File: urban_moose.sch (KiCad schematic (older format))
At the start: 52 parts, among them P1 SWD, P2 EXT, P3 ANT, Q1 MOSFET_N, Q2 MOSFET_N, SW1 SW_PUSH, U1 nRF51822-QFAA, U2 DS18B20, U3 BMP180, U4 Si1145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

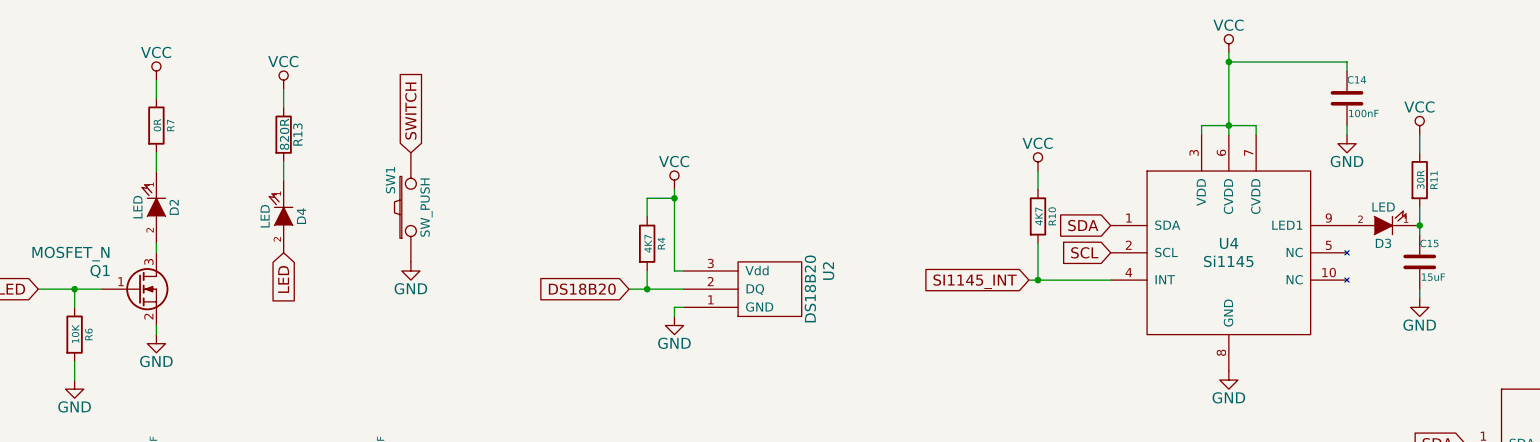
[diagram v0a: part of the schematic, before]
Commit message: Fixes to match library changes
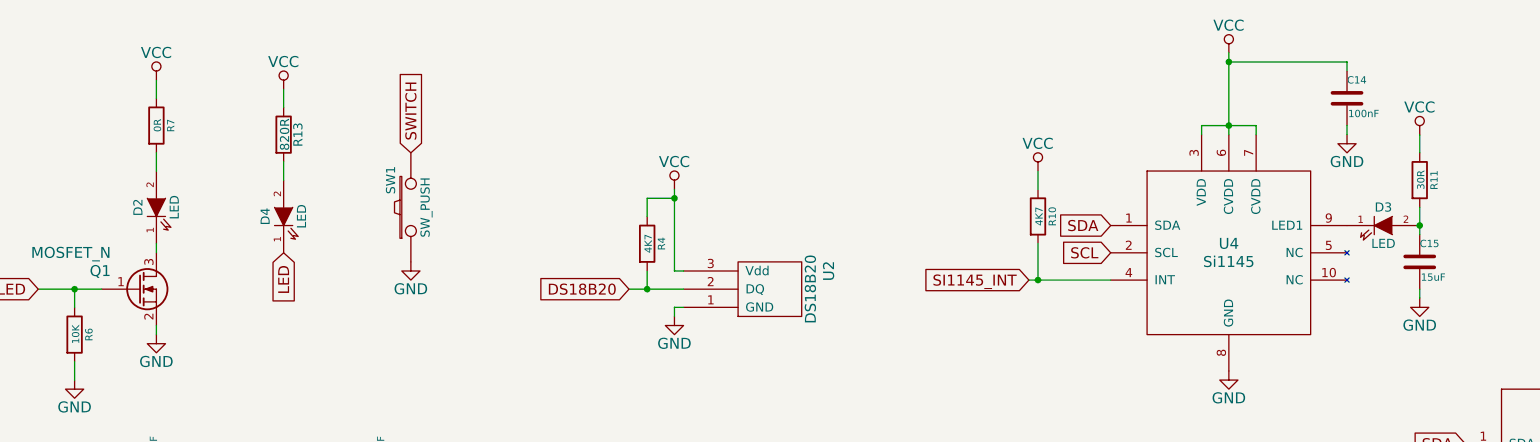
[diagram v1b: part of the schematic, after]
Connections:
- net LED: now also D4.1 (K); no longer D4.2 (A)
- net at D2.1 (K): now also Q1.3 (D); no longer R7.2
- net at D2.2 (A): now also R7.2; no longer Q1.3 (D)
- net at U4.9 (LED1): now also D3.1 (K); no longer D3.2 (A)
- net at C15.1, R11.2: now also D3.2 (A); no longer D3.1 (K)
- net at R13.2: now also D4.2 (A); no longer D4.1 (K)
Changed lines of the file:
@@
 LIBS:memory
 LIBS:xilinx
-LIBS:special
 LIBS:microcontrollers
 LIBS:dsp
@@
 F 3 "" H 1850 1700 60  0000 C CNN
 	1    1850 1700
-	0    1    1    0
+	0    -1   -1   0
 $EndComp
 $Comp
@@
 F 3 "" H 8600 1800 60  0000 C CNN
 	1    8600 1800
-	-1   0    0    1
+	1    0    0    -1
 $EndComp
 $Comp
@@
 F 3 "" H 2550 1750 60  0000 C CNN
 	1    2550 1750
-	0    1    1    0
-$EndComp
-$Comp
+	0    -1   -1   0
+$EndComp
+$Comp

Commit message: Change footprint for nRF51 to the correct pitch
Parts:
- U1: footprint Housings_DFN_QFN:QFN-48-1EP_7x7mm_Pitch0.5mm -> Housings_DFN_QFN:UQFN-48-1EP_6x6mm_Pitch0.4mm
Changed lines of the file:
@@
 F 0 "U1" H 3200 5450 60  0000 C CNN
 F 1 "nRF51822-QFAA" H 3200 5350 60  0000 C CNN
-F 2 "Housings_DFN_QFN:QFN-48-1EP_7x7mm_Pitch0.5mm" H 3250 5300 60  0001 C CNN
+F 2 "Housings_DFN_QFN:UQFN-48-1EP_6x6mm_Pitch0.4mm" H 3250 5300 60  0001 C CNN
 F 3 "" H 3250 5300 60  0000 C CNN
 	1    3200 5400

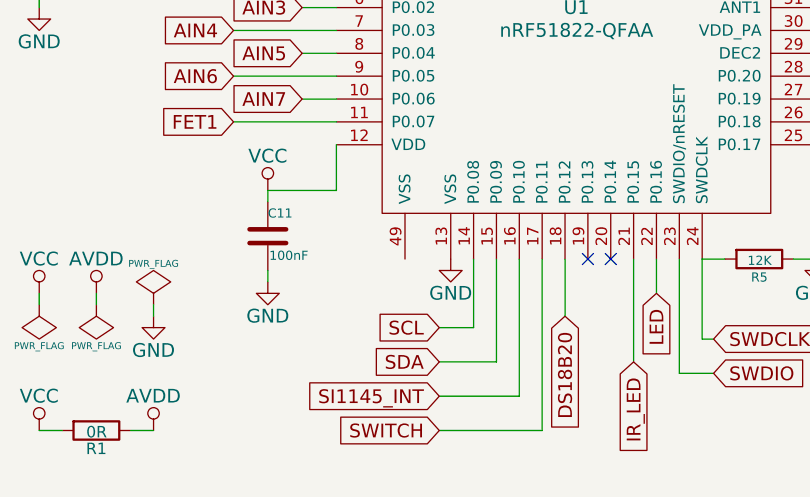
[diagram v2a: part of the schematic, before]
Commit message: Connect nRF51 centre pad and add vias
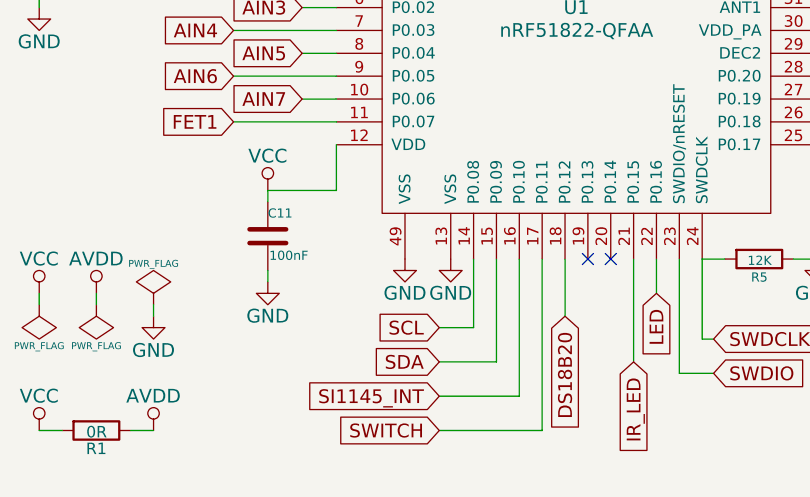
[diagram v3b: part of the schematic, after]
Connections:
- net GND: now also U1.49 (VSS)
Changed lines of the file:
@@
 Wire Wire Line
 	7700 3600 7500 3600
+$Comp
+L GND #PWR?
+U 1 1 56397618
+P 2450 6450
+F 0 "#PWR?" H 2450 6200 60  0001 C CNN
+F 1 "GND" H 2450 6300 60  0000 C CNN
+F 2 "" H 2450 6450 60  0000 C CNN
+F 3 "" H 2450 6450 60  0000 C CNN
+	1    2450 6450
+	1    0    0    -1
+$EndComp
 $EndSCHEMATC
